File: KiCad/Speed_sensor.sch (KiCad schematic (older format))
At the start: 56 parts

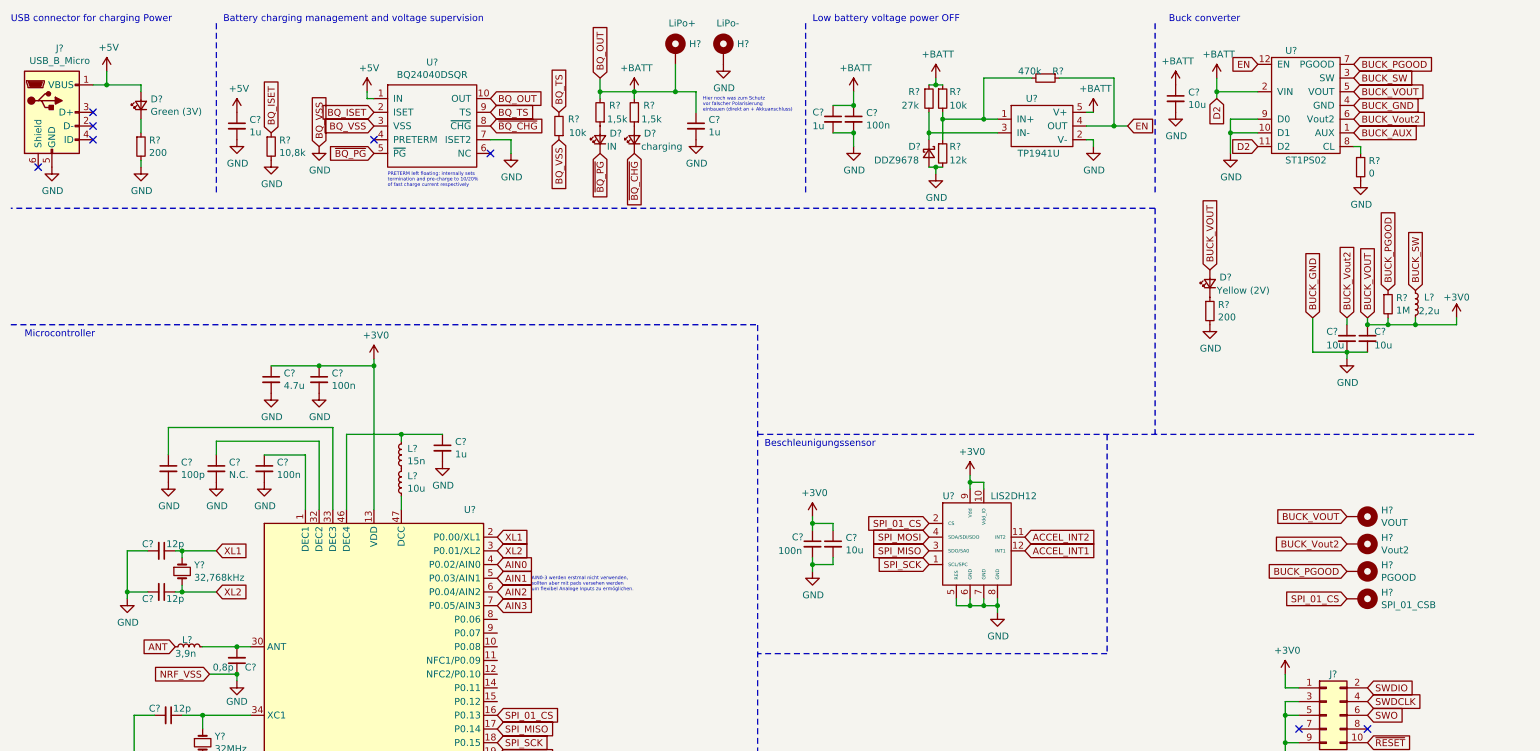
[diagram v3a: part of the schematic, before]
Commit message: antenna added
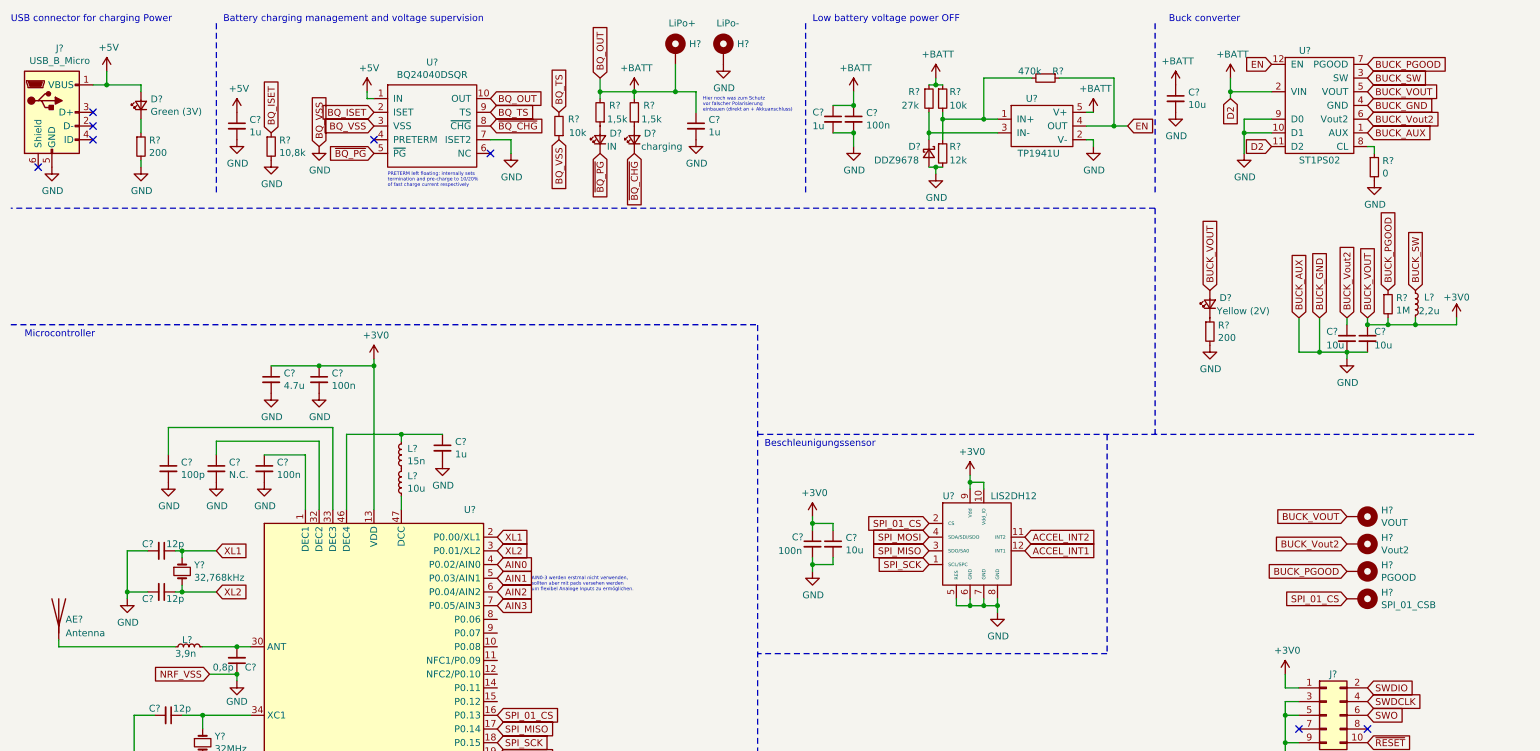
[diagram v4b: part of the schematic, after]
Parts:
- added AE?: Antenna, symbol Device:Antenna
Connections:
- net BUCK_AUX is gone; now on net GND: U?.1 (AUX)
- net ANT: no longer names the net of L?.1
- net ANT: now also AE?.1 (A)
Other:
- moved on the sheet: D?, R?, U?
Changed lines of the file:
@@
 Text Notes 600  2900 0    50   ~ 0
 Microcontroller
-Text GLabel 1700 5150 0    50   Input ~ 0
-ANT
 Text GLabel 10250 4200 0    50   Input ~ 0
 BUCK_VOUT
@@
 Text GLabel 10400 5650 2    50   Input ~ 0
 SWO
-Text GLabel 9600 1500 0    50   Input ~ 0
+Text GLabel 9700 1500 0    50   Input ~ 0
 D2
-Text GLabel 9600 900  0    50   Input ~ 0
+Text GLabel 9700 900  0    50   Input ~ 0
 EN
 $Comp
@@
 L Device:LED_Small D?
 U 1 1 6089BF8D
-P 9250 2500
+P 9250 2650
 AR Path="/608A57BF/6089BF8D" Ref="D?"  Part="1"
 AR Path="/6089BF8D" Ref="D?"  Part="1"
-F 0 "D?" V 9296 2430 50  0000 R CNN
-F 1 "Yellow (2V)" V 9200 2450 50  0000 R CNN
-F 2 "" V 9250 2500 50  0001 C CNN
-F 3 "~" V 9250 2500 50  0001 C CNN
-	1    9250 2500
+F 0 "D?" V 9296 2580 50  0000 R CNN
+F 1 "Yellow (2V)" V 9200 2600 50  0000 R CNN
+F 2 "" V 9250 2650 50  0001 C CNN
+F 3 "~" V 9250 2650 50  0001 C CNN
+	1    9250 2650
 	0    -1   -1   0
 $EndComp
@@
 L Device:R_Small R?
 U 1 1 6089BF93
-P 9250 2700
+P 9250 2850
 AR Path="/608A57BF/6089BF93" Ref="R?"  Part="1"
 AR Path="/6089BF93" Ref="R?"  Part="1"
-F 0 "R?" H 9309 2746 50  0000 L CNN
-F 1 "200" H 9309 2655 50  0000 L CNN
-F 2 "" H 9250 2700 50  0001 C CNN
-F 3 "~" H 9250 2700 50  0001 C CNN
-	1    9250 2700
+F 0 "R?" H 9309 2896 50  0000 L CNN
+F 1 "200" H 9309 2805 50  0000 L CNN
+F 2 "" H 9250 2850 50  0001 C CNN
+F 3 "~" H 9250 2850 50  0001 C CNN
+	1    9250 2850
 	1    0    0    -1
 $EndComp
@@
 L power:GND #PWR?
 U 1 1 6089BF99
-P 9250 2800
+P 9250 2950
 AR Path="/608A57BF/6089BF99" Ref="#PWR?"  Part="1"
 AR Path="/6089BF99" Ref="#PWR?"  Part="1"
-F 0 "#PWR?" H 9250 2550 50  0001 C CNN
-F 1 "GND" H 9255 2627 50  0000 C CNN
-F 2 "" H 9250 2800 50  0001 C CNN
-F 3 "" H 9250 2800 50  0001 C CNN
-	1    9250 2800
+F 0 "#PWR?" H 9250 2700 50  0001 C CNN
+F 1 "GND" H 9255 2777 50  0000 C CNN
+F 2 "" H 9250 2950 50  0001 C CNN
+F 3 "" H 9250 2950 50  0001 C CNN
+	1    9250 2950
 	1    0    0    -1
 $EndComp
@@
 L power:+BATT #PWR?
 U 1 1 6089BFA9
-P 9300 1000
+P 9400 1000
 AR Path="/6089BFA9" Ref="#PWR?"  Part="1"
 AR Path="/608A57BF/6089BFA9" Ref="#PWR?"  Part="1"
-F 0 "#PWR?" H 9300 850 50  0001 C CNN
-F 1 "+BATT" H 9315 1173 50  0000 C CNN
-F 2 "" H 9300 1000 50  0001 C CNN
-F 3 "" H 9300 1000 50  0001 C CNN
-	1    9300 1000
+F 0 "#PWR?" H 9400 850 50  0001 C CNN
+F 1 "+BATT" H 9415 1173 50  0000 C CNN
+F 2 "" H 9400 1000 50  0001 C CNN
+F 3 "" H 9400 1000 50  0001 C CNN
+	1    9400 1000
 	1    0    0    -1
 $EndComp
@@
 L Nils_KiCADLibrary:ST1PS02 U?
 U 1 1 609A8A46
-P 9950 1200
+P 10050 1200
 AR Path="/609A8A46" Ref="U?"  Part="1"
 AR Path="/608A57BF/609A8A46" Ref="U?"  Part="1"
-F 0 "U?" H 9800 1600 50  0000 L CNN
-F 1 "ST1PS02" H 9800 800 50  0000 L CNN
-F 2 "" H 10050 1100 50  0001 C CNN
-F 3 "" H 10050 1100 50  0001 C CNN
-	1    9950 1200
+F 0 "U?" H 9900 1600 50  0000 L CNN
+F 1 "ST1PS02" H 9900 800 50  0000 L CNN
+F 2 "" H 10150 1100 50  0001 C CNN
+F 3 "" H 10150 1100 50  0001 C CNN
+	1    10050 1200
 	1    0    0    -1
 $EndComp
@@
 Text Notes 8950 600  0    50   ~ 0
 Buck converter
-Text GLabel 9300 1150 3    50   Input ~ 0
+Text GLabel 9400 1150 3    50   Input ~ 0
 D2
 $Comp
 L power:GND #PWR?
 U 1 1 609EC4A9
-P 9400 1550
+P 9500 1550
 AR Path="/608A57BF/609EC4A9" Ref="#PWR?"  Part="1"
 AR Path="/609EC4A9" Ref="#PWR?"  Part="1"
-F 0 "#PWR?" H 9400 1300 50  0001 C CNN
-F 1 "GND" H 9405 1377 50  0000 C CNN
-F 2 "" H 9400 1550 50  0001 C CNN
-F 3 "" H 9400 1550 50  0001 C CNN
-	1    9400 1550
-	1    0    0    -1
-$EndComp
-Wire Wire Line
-	9400 1400 9600 1400
-Wire Wire Line
-	9400 1300 9400 1400
-Connection ~ 9400 1400
-Wire Wire Line
-	9400 1400 9400 1550
-Text GLabel 10300 1100 2    50   Input ~ 0
+F 0 "#PWR?" H 9500 1300 50  0001 C CNN
+F 1 "GND" H 9505 1377 50  0000 C CNN
+F 2 "" H 9500 1550 50  0001 C CNN
+F 3 "" H 9500 1550 50  0001 C CNN
+	1    9500 1550
+	1    0    0    -1
+$EndComp
+Wire Wire Line
+	9500 1400 9700 1400
+Wire Wire Line
+	9500 1300 9500 1400
+Connection ~ 9500 1400
+Wire Wire Line
+	9500 1400 9500 1550
+Text GLabel 10400 1100 2    50   Input ~ 0
 BUCK_VOUT
-Text GLabel 9250 2400 1    50   Input ~ 0
+Text GLabel 9250 2550 1    50   Input ~ 0
 BUCK_VOUT
 Wire Wire Line
-	9400 1300 9600 1300
-Wire Wire Line
-	9300 1000 9300 1100
-Wire Wire Line
-	9300 1100 9600 1100
-Connection ~ 9300 1100
-Wire Wire Line
-	9300 1100 9300 1150
+	9500 1300 9700 1300
+Wire Wire Line
+	9400 1000 9400 1100
+Wire Wire Line
+	9400 1100 9700 1100
+Connection ~ 9400 1100
+Wire Wire Line
+	9400 1100 9400 1150
 $Comp
 L Device:C_Small C?
@@
 	1    0    0    -1
 $EndComp
-Text GLabel 10300 900  2    50   Input ~ 0
+Text GLabel 10400 900  2    50   Input ~ 0
 BUCK_PGOOD
-Text GLabel 10300 1000 2    50   Input ~ 0
+Text GLabel 10400 1000 2    50   Input ~ 0
 BUCK_SW
-Text GLabel 10300 1200 2    50   Input ~ 0
+Text GLabel 10400 1200 2    50   Input ~ 0
 BUCK_GND
-Text GLabel 10300 1300 2    50   Input ~ 0
+Text GLabel 10400 1300 2    50   Input ~ 0
 BUCK_Vout2
-Text GLabel 10300 1400 2    50   Input ~ 0
+Text GLabel 10400 1400 2    50   Input ~ 0
 BUCK_AUX
 $Comp
 L Device:R_Small R?
 U 1 1 60A65878
-P 10350 1650
+P 10450 1650
 AR Path="/608A57BF/60A65878" Ref="R?"  Part="1"
 AR Path="/60A65878" Ref="R?"  Part="1"
-F 0 "R?" H 10409 1696 50  0000 L CNN
-F 1 "0" H 10409 1605 50  0000 L CNN
-F 2 "" H 10350 1650 50  0001 C CNN
-F 3 "~" H 10350 1650 50  0001 C CNN
-	1    10350 1650
+F 0 "R?" H 10509 1696 50  0000 L CNN
+F 1 "0" H 10509 1605 50  0000 L CNN
+F 2 "" H 10450 1650 50  0001 C CNN
+F 3 "~" H 10450 1650 50  0001 C CNN
+	1    10450 1650
 	1    0    0    -1
 $EndComp
@@
 L power:GND #PWR?
 U 1 1 60A65B79
-P 10350 1750
+P 10450 1750
 AR Path="/608A57BF/60A65B79" Ref="#PWR?"  Part="1"
 AR Path="/60A65B79" Ref="#PWR?"  Part="1"
-F 0 "#PWR?" H 10350 1500 50  0001 C CNN
-F 1 "GND" H 10355 1577 50  0000 C CNN
-F 2 "" H 10350 1750 50  0001 C CNN
-F 3 "" H 10350 1750 50  0001 C CNN
-	1    10350 1750
-	1    0    0    -1
-$EndComp
-Wire Wire Line
-	10350 1550 10350 1500
-Wire Wire Line
-	10350 1500 10300 1500
+F 0 "#PWR?" H 10450 1500 50  0001 C CNN
+F 1 "GND" H 10455 1577 50  0000 C CNN
+F 2 "" H 10450 1750 50  0001 C CNN
+F 3 "" H 10450 1750 50  0001 C CNN
+	1    10450 1750
+	1    0    0    -1
+$EndComp
+Wire Wire Line
+	10450 1550 10450 1500
+Wire Wire Line
+	10450 1500 10400 1500
 Wire Wire Line
 	3150 3100 3150 4150
@@
 Text GLabel 10400 2750 1    50   Input ~ 0
 BUCK_VOUT
-Text GLabel 10000 2750 1    50   Input ~ 0
+Text GLabel 10050 2750 1    50   Input ~ 0
 BUCK_GND
 Text GLabel 10250 2750 1    50   Input ~ 0
@@
 Connection ~ 10400 2800
 Wire Wire Line
-	10000 2750 10000 3000
-Wire Wire Line
-	10000 3000 10250 3000
+	10050 2750 10050 3000
 $Comp
 L Device:L_Small L?
@@
 Wire Wire Line
 	10750 2800 11050 2800
+Connection ~ 10050 3000
+Wire Wire Line
+	10050 3000 10250 3000
+Text GLabel 9900 2750 1    50   Input ~ 0
+BUCK_AUX
+Wire Wire Line
+	9900 2750 9900 3000
+Wire Wire Line
+	9900 3000 10050 3000
+$Comp
+L Device:Antenna AE?
+U 1 1 60D47EFA
+P 850 4900
+F 0 "AE?" H 900 4850 50  0000 L CNN
+F 1 "Antenna" H 900 4750 50  0000 L CNN
+F 2 "" H 850 4900 50  0001 C CNN
+F 3 "~" H 850 4900 50  0001 C CNN
+	1    850  4900
+	1    0    0    -1
+$EndComp
+Wire Wire Line
+	1700 5150 850  5150
+Wire Wire Line
+	850  5150 850  5100
 $EndSCHEMATC

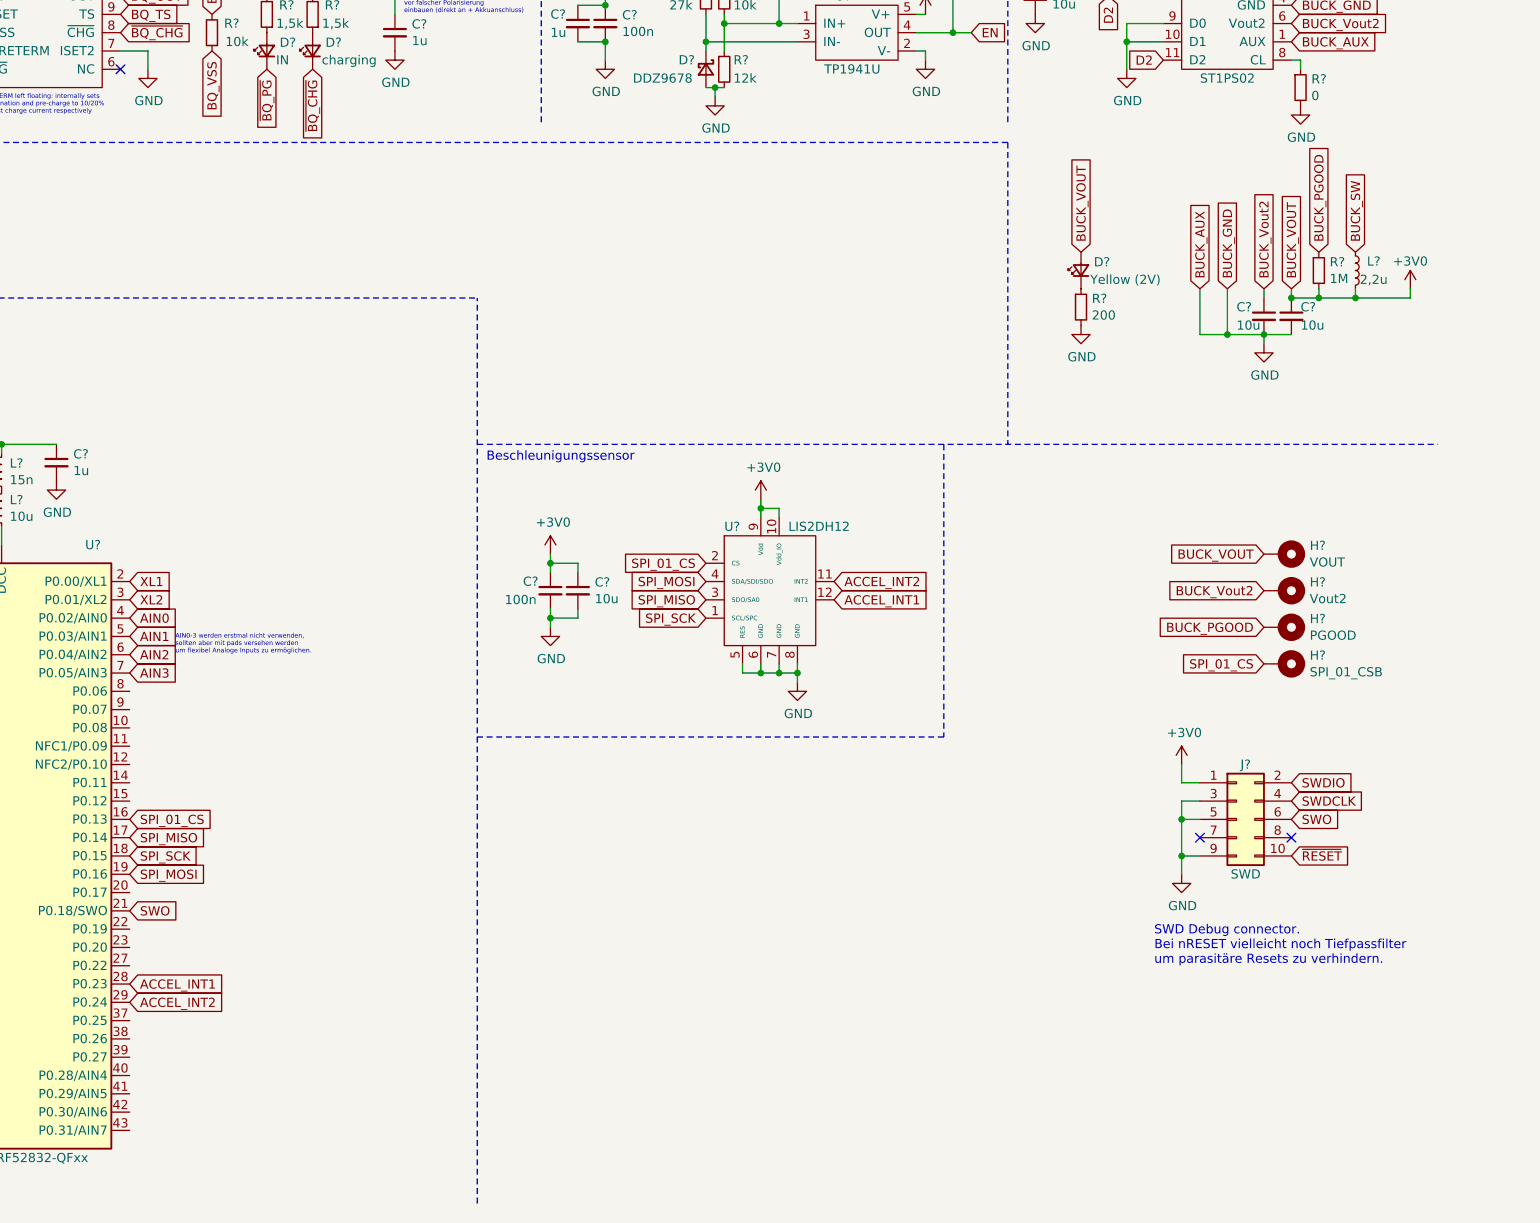
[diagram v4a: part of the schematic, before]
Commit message: added pads for all AINx, decided on which GPIO to use (wil prop change again)
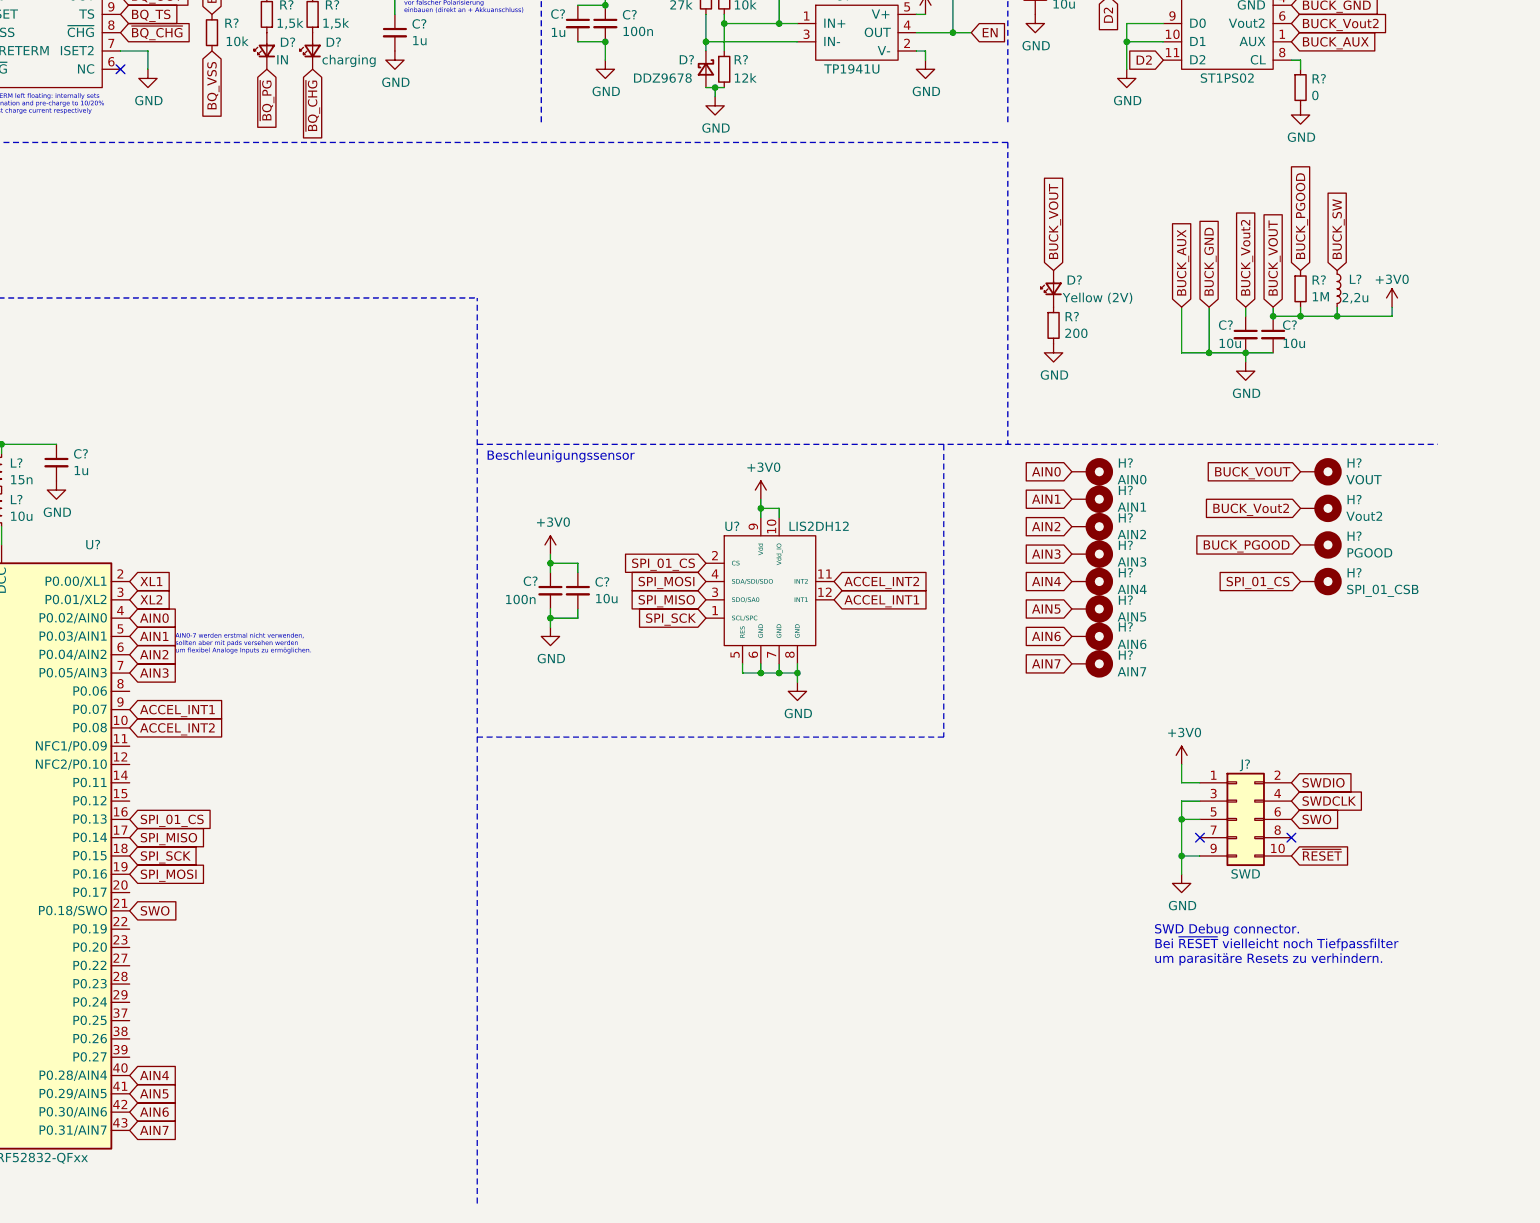
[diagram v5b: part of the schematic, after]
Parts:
- added H?: AIN0, symbol Mechanical:MountingHole_Pad
- added H?: AIN1, symbol Mechanical:MountingHole_Pad
- added H?: AIN2, symbol Mechanical:MountingHole_Pad
- added H?: AIN3, symbol Mechanical:MountingHole_Pad
- added H?: AIN4, symbol Mechanical:MountingHole_Pad
- added H?: AIN5, symbol Mechanical:MountingHole_Pad
- added H?: AIN6, symbol Mechanical:MountingHole_Pad
- added H?: AIN7, symbol Mechanical:MountingHole_Pad
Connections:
- net ACCEL_INT1: now also U?.9 (P0.07); no longer U?.28 (P0.23)
- net ACCEL_INT2: now also U?.10 (P0.08); no longer U?.29 (P0.24)
- net AIN0: now also H?.1
- net AIN1: now also H?.1
- net AIN2: now also H?.1
- net AIN3: now also H?.1
- net AIN4: now reaches U?.40 (P0.28/AIN4)
- net AIN4: now also H?.1
- net AIN5: now reaches U?.41 (P0.29/AIN5)
- net AIN5: now also H?.1
- net AIN6: now reaches U?.42 (P0.30/AIN6)
- net AIN6: now also H?.1
- net AIN7: now reaches U?.43 (P0.31/AIN7)
- net AIN7: now also H?.1
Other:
- note added: "AIN0-7 werden erstmal nicht verwenden, \nsollten aber mit pads versehen werden \num flexibel Analoge Inputs zu ermöglichen."
- note added: "SWD Debug connector.\nBei ~RESET~ vielleicht noch Tiefpassfilter\num parasitäre Resets zu verhindern."
- note removed: "AIN0-3 werden erstmal nicht verwenden, \nsollten aber mit pads versehen werden \num flexibel Analoge Inputs zu ermöglichen."
- note removed: "SWD Debug connector.\nBei nRESET vielleicht noch Tiefpassfilter\num parasitäre Resets zu verhindern."
- moved on the sheet: C?, D?, H?, L?, R?

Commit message: added small comment)
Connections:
- no-connect marks 8 -> 22
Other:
- note added: "Next step: Choose all the correct footprints!!!"
- note removed: "AIN0-7 werden erstmal nicht verwenden, \nsollten aber mit pads versehen werden \num flexibel Analoge Inputs zu ermöglichen."
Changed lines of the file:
@@
 Text GLabel 4050 4850 2    50   Input ~ 0
 AIN3
-Text Notes 4300 4750 0    25   ~ 0
-AIN0-7 werden erstmal nicht verwenden, \nsollten aber mit pads versehen werden \num flexibel Analoge Inputs zu ermöglichen.
 Text GLabel 2000 4450 2    50   Input ~ 0
 XL1
@@
 Text GLabel 9200 4800 0    50   Input ~ 0
 AIN7
+NoConn ~ 4050 4950
+NoConn ~ 4050 5250
+NoConn ~ 4050 5350
+NoConn ~ 4050 5450
+NoConn ~ 4050 5550
+NoConn ~ 4050 6050
+NoConn ~ 4050 6250
+NoConn ~ 4050 6350
+NoConn ~ 4050 6450
+NoConn ~ 4050 6550
+NoConn ~ 4050 6650
+NoConn ~ 4050 6750
+NoConn ~ 4050 6850
+NoConn ~ 4050 6950
+Text Notes 1750 2450 0    157  Italic 31
+Next step: Choose all the correct footprints!!!
 $EndSCHEMATC
